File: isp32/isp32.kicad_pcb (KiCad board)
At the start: 2 copper layers, 55.5 x 48.5 mm, 99 parts, among them J1 BAT1, J10 LoRa_ANT, J12 Micro_SD_Card, J2 Switching, J3 USB_C_Receptacle_USB2.0, J4 ESP_JTAG, J5 GPS_ANT, J6 F0, J7 F1, J9 ANT, M1 Motor_Servo, M2 Motor_Servo, M3 Motor_Servo, M4 Motor_Servo, Q1 BSS138, Q2 BSS138, Q3 IRLML6402, Q4 BSS138, Q5 IRLML6402, Q6 S8050, SW1 RST, SW2 IO0, U1 SC189ZSKTRT, U10 BMP280, U11 MPU-9250, U2 USBLC6-2SC6, U3 STM32F030F4Px, U4 MP1660GTF-Z, U6 24LC32, U7 NEO-XM, U8 ESP32-S3-WROOM-1U, U9 RFM98W-315S2

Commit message: Rough route
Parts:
- added REF**: OSHW-Logo2_7.3x6mm_SilkScreen, Symbol:OSHW-Logo2_7.3x6mm_SilkScreen, F.Cu at (110.5, 79.2)
- C1, C10, C6, G***, L1, U1: moved to F.Cu
- C2, C4, C5, C7, C8, L3, LS1, Q6, R10, R11, R3, R33, R8, R9, TP2, U4: moved to B.Cu
- U3: value STM32F030F4Px -> STM32G030F6
- moved C10 48.5 mm to (123.2, 76.3)
- moved R10 45.8 mm to (118.8, 84.4), turned to -90 degrees
- moved G*** 45.7 mm to (129.8, 75.1), turned to 0 degrees
- moved R9 43.8 mm to (117.2, 84.4), turned to -90 degrees
- moved C6 42.5 mm to (120.2, 77.1)
- moved R11 42.4 mm to (118.5, 82.0), turned to 0 degrees
- moved R3 41.9 mm to (115.5, 84.4), turned to 90 degrees
- moved C7 40.6 mm to (118.5, 80.3), turned to 0 degrees
- moved C5 39.7 mm to (113.6, 84.4), turned to -90 degrees
- moved C3 39.3 mm to (121.3, 59.7), turned to -90 degrees
- moved R33 39.1 mm to (115.0, 62.7)
- moved Q6 38.2 mm to (114.9, 65.6), turned to -90 degrees
- moved U4 37.9 mm to (115.3, 81.2), turned to 0 degrees
- moved C13 37.0 mm to (138.7, 59.3)
- moved U6 36.9 mm to (133.7, 58.0)
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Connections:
- U3 pad 1: GND -> SCL
- U3 pad 11: unconnected-(U3-Pad11) -> SERVO0
- U3 pad 12: unconnected-(U3-Pad12) -> SERVO1
- U3 pad 13: unconnected-(U3-Pad13) -> SERVO2
- U3 pad 14: unconnected-(U3-Pad14) -> SERVO3
- U3 pad 15: GND -> unconnected-(U3-Pad15)
- U3 pad 16: +3V3 -> unconnected-(U3-Pad16)
- U3 pad 17: SCL -> unconnected-(U3-Pad17)
- U3 pad 18: SDA -> SWDIO
- U3 pad 19: SWDIO -> SWCLK
- U3 pad 2: unconnected-(U3-Pad2) -> SDA
- U3 pad 20: SWCLK -> unconnected-(U3-Pad20)
- U3 pad 4: RST -> +3V3
- U3 pad 5: +3V3 -> GND
- U3 pad 6: SERVO0 -> RST
- U3 pad 7: SERVO1 -> Buzz
- U3 pad 8: SERVO2 -> RGB
- U3 pad 9: SERVO3 -> unconnected-(U3-Pad9)
- U8 pad 39: Buzz -> unconnected-(U8-Pad39)
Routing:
- net +3V3: track 9.51 -> 239.7 mm, vias 0 -> 9
- net +5V: track 25.5 -> 163.7 mm, vias 1 -> 2
- net +BATT: track 10.8 -> 42.2 mm, vias 0 -> 1
- net IMU_INT: track 0.00 -> 14.4 mm
- net Net-(J10-Pad1): track 0.00 -> 11.4 mm, vias 0 -> 1
- net MISO: track 0.00 -> 11.0 mm
- net Net-(J6-Pad1): track 0.00 -> 8.88 mm
- net Net-(J7-Pad1): track 0.00 -> 8.70 mm
- net SCL: track 0.00 -> 8.30 mm
- net SDA: track 0.00 -> 6.84 mm
- net Net-(Q1-Pad3): track 0.00 -> 5.52 mm
- net Net-(Q4-Pad3): track 0.00 -> 5.52 mm
- net Net-(D3-Pad2): track 0.00 -> 5.38 mm
- net UD+: track 0.00 -> 5.15 mm
- net cc1: track 0.00 -> 5.09 mm, vias 0 -> 2
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- added copper zone on F.Cu, net +3V3
- added copper zone on B.Cu, net +5V
- added copper zone on F.Cu, net +5V
- added copper zone on B.Cu, net +BATT
- added copper zone on B.Cu, net Net-(C4-Pad2)
- added copper zone on F.Cu, net Net-(L1-Pad1)
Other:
- board size 55.5 x 48.5 mm -> 53 x 48 mm
- board text added: "Board's Info 48mm x 53mm M3 Screwhole Input 5V~16V BSD-3-Clause By @wilicw"

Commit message: Complete routing
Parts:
- R19: moved to B.Cu
- moved R19 2.18 mm to (108.6, 84.9)
- moved REF** 0.78 mm to (110.7, 80.0)
- moved G*** 0.08 mm to (129.8, 75.0)
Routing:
- net MOSI: track 1.34 -> 67.2 mm, vias 0 -> 4
- net SDA: track 6.84 -> 63.0 mm, vias 0 -> 5
- net SCL: track 8.30 -> 59.3 mm, vias 0 -> 4
- net MISO: track 11.0 -> 61.0 mm, vias 0 -> 4
- net SCK: track 1.33 -> 50.2 mm, vias 0 -> 2
- net EXT_INT: track 0.00 -> 45.7 mm, vias 0 -> 2
- net GND: track 0.53 -> 37.6 mm, vias 3 -> 474
- net LORA_SS: track 0.00 -> 32.2 mm, vias 0 -> 1
- net IO0: track 2.06 -> 32.3 mm, vias 1 -> 2
- net RGB: track 1.97 -> 30.6 mm, vias 0 -> 2
- net LORA_INT: track 0.00 -> 26.4 mm, vias 0 -> 1
- net FIRE0: track 1.99 -> 24.9 mm, vias 0 -> 2
- net RST: track 0.00 -> 21.7 mm, vias 0 -> 1
- net TX1: track 0.00 -> 21.0 mm, vias 0 -> 2
- net SERVO3: track 0.00 -> 20.9 mm
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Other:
- board text added: "Board's Info 48mm x 53mm M3 Screw Holes Input 5V~16V BSD-3-Clause By @wilicw"
- board text removed: "Board's Info 48mm x 53mm M3 Screwhole Input 5V~16V BSD-3-Clause By @wilicw"

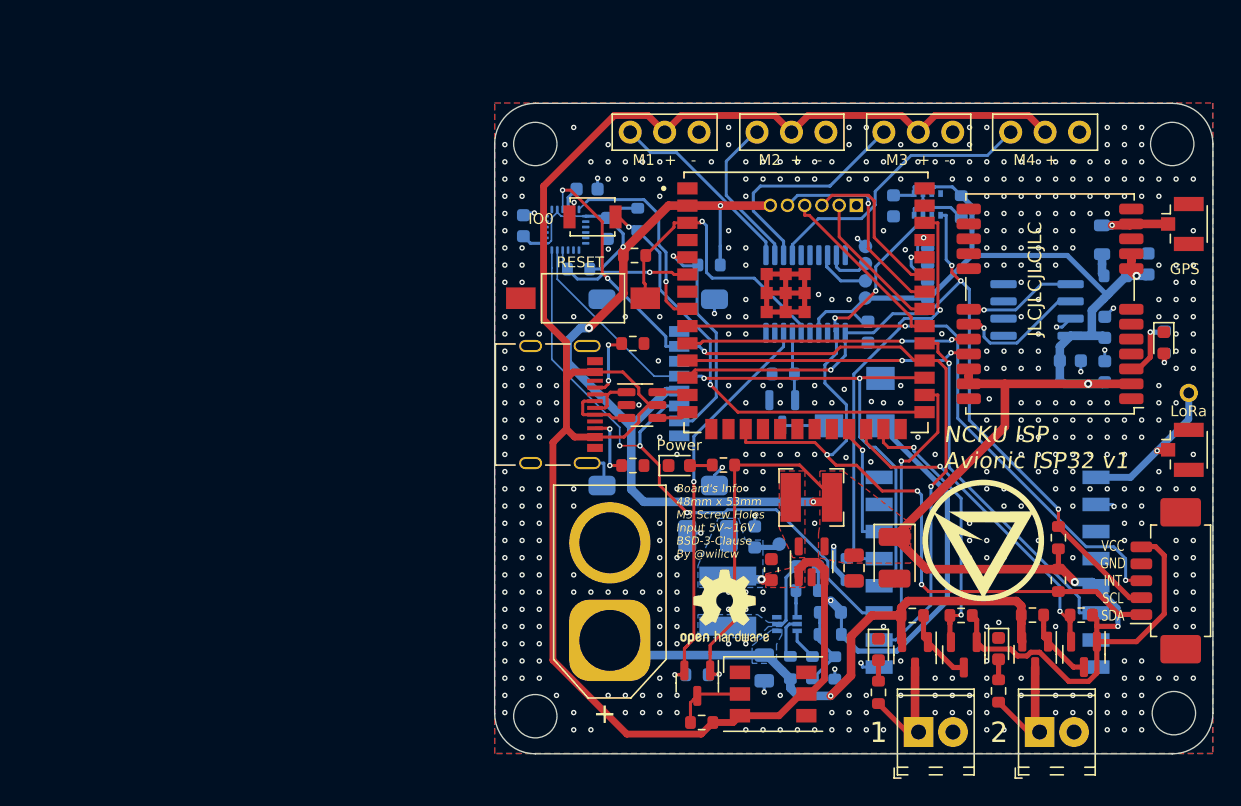
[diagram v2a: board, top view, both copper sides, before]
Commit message: Change label style
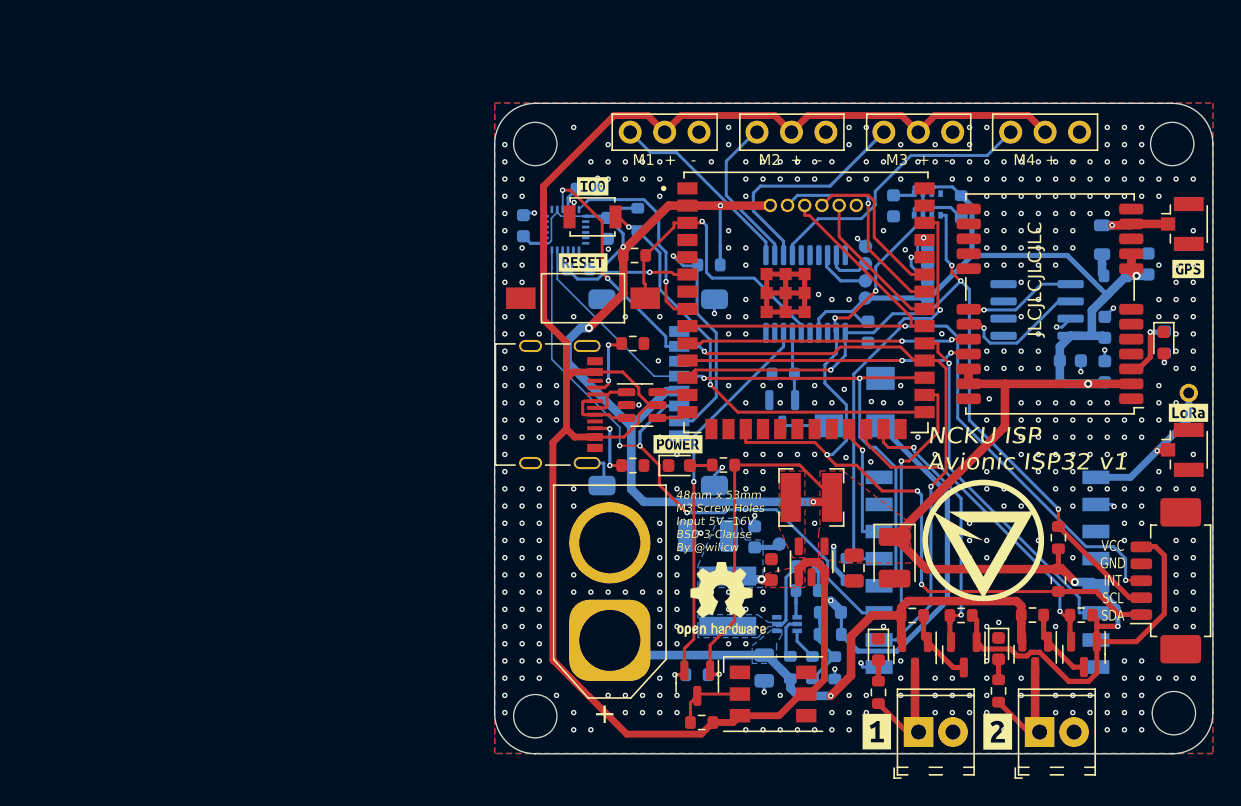
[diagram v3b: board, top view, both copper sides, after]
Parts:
- added kibuzzard-63CD04EB: G***, kibuzzard-63CD04EB, F.Cu at (121.9, 89.1)
- added kibuzzard-63CD04FB: G***, kibuzzard-63CD04FB, F.Cu at (130.8, 89.1)
- added kibuzzard-63CD1CED: G***, kibuzzard-63CD1CED, F.Cu at (100.2, 54.5)
- added kibuzzard-63CD1CF7: G***, kibuzzard-63CD1CF7, F.Cu at (100.9, 48.9)
- added kibuzzard-63CD1D24: G***, kibuzzard-63CD1D24, F.Cu at (107.2, 67.9)
- added kibuzzard-63CD1D2E: G***, kibuzzard-63CD1D2E, F.Cu at (144.9, 65.6)
- added kibuzzard-63CD1D37: G***, kibuzzard-63CD1D37, F.Cu at (144.9, 55.0)
- added kibuzzard-63CD1E61: G***, kibuzzard-63CD1E61, B.Cu at (123.0, 57.1)
- added kibuzzard-63CD1E61: G***, kibuzzard-63CD1E61, B.Cu at (127.6, 57.2)
- added kibuzzard-63CD1E6C: G***, kibuzzard-63CD1E6C, B.Cu at (127.6, 55.9)
- added kibuzzard-63CD1E76: G***, kibuzzard-63CD1E76, B.Cu at (127.6, 54.6)
- added kibuzzard-63CD1E7F: G***, kibuzzard-63CD1E7F, B.Cu at (127.6, 53.4)
- added kibuzzard-63CD1E7F: G***, kibuzzard-63CD1E7F, B.Cu at (123.0, 53.3)
- added kibuzzard-63CD1EC0: G***, kibuzzard-63CD1EC0, B.Cu at (123.0, 54.6)
- added kibuzzard-63CD1EC5: G***, kibuzzard-63CD1EC5, B.Cu at (123.0, 55.9)
- added kibuzzard-63CD1F56: G***, kibuzzard-63CD1F56, B.Cu at (120.4, 48.4)
- added kibuzzard-63CD1F64: G***, kibuzzard-63CD1F64, B.Cu at (119.1, 48.4)
- added kibuzzard-63CD1F6A: G***, kibuzzard-63CD1F6A, B.Cu at (117.9, 48.4)
- added kibuzzard-63CD1F72: G***, kibuzzard-63CD1F72, B.Cu at (116.6, 48.4)
- added kibuzzard-63CD1F77: G***, kibuzzard-63CD1F77, B.Cu at (115.3, 48.4)
- added kibuzzard-63CD1F7D: G***, kibuzzard-63CD1F7D, B.Cu at (114.0, 48.4)
- moved REF** 0.61 mm to (110.4, 79.4)
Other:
- board text added: "48mm x 53mm M3 Screw Holes Input 5V~16V BSD-3-Clause By @wilicw"
- board text added: "Designed in ROC (Taiwan)"
- board text removed: "1"
- board text removed: "2"
- board text removed: "Board's Info 48mm x 53mm M3 Screw Holes Input 5V~16V BSD-3-Clause By @wilicw"
- board text removed: "GND RXD TXD 3V3"
- board text removed: "GND SWCLK SWDIO 3V3"
- board text removed: "GND TDO TMS TCK TDI 3V3"
- board text removed: "GPS"
- board text removed: "IO0"
- board text removed: "LoRa"
- board text removed: "Power"
- board text removed: "RESET"

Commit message: Change label and panel size
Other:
- board text removed: "Designed in ROC (Taiwan)"
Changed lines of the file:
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@@
     (attr board_only exclude_from_pos_files exclude_from_bom)
     (fp_text reference "kibuzzard-63CD1D37" (at 0 -3.722793) (layer "F.SilkS") hide
-      (effects (font (size 0 0)))
+      (effects (font (size 0 0) (thickness 0.15)))
     )
     (fp_text value "G***" (at 0 3.722793) (layer "F.SilkS") hide
-      (effects (font (size 0 0)))
+      (effects (font (size 0 0) (thickness 0.15)))
     )
     (fp_poly (pts
@@
     (attr board_only exclude_from_pos_files exclude_from_bom)
     (fp_text reference "kibuzzard-63CD1CED" (at 0 -3.722793) (layer "F.SilkS") hide
-      (effects (font (size 0 0)))
+      (effects (font (size 0 0) (thickness 0.15)))
     )
     (fp_text value "G***" (at 0 3.722793) (layer "F.SilkS") hide
-      (effects (font (size 0 0)))
+      (effects (font (size 0 0) (thickness 0.15)))
     )
     (fp_poly (pts
@@
     (attr board_only exclude_from_pos_files exclude_from_bom)
     (fp_text reference "kibuzzard-63CD1CF7" (at 0 -3.722793) (layer "F.SilkS") hide
-      (effects (font (size 0 0)))
+      (effects (font (size 0 0) (thickness 0.15)))
     )
     (fp_text value "G***" (at 0 3.722793) (layer "F.SilkS") hide
-      (effects (font (size 0 0)))
+      (effects (font (size 0 0) (thickness 0.15)))
     )
     (fp_poly (pts
@@
     (attr board_only exclude_from_pos_files exclude_from_bom)
     (fp_text reference "kibuzzard-63CD1D2E" (at 0 -3.718348) (layer "F.SilkS") hide
-      (effects (font (size 0 0)))
+      (effects (font (size 0 0) (thickness 0.15)))
     )
     (fp_text value "G***" (at 0 3.718348) (layer "F.SilkS") hide
-      (effects (font (size 0 0)))
+      (effects (font (size 0 0) (thickness 0.15)))
     )
     (fp_poly (pts
@@
     (attr board_only exclude_from_pos_files exclude_from_bom)
     (fp_text reference "kibuzzard-63CD1D24" (at 0 -3.722793) (layer "F.SilkS") hide
-      (effects (font (size 0 0)))
+      (effects (font (size 0 0) (thickness 0.15)))
     )
     (fp_text value "G***" (at 0 3.722793) (layer "F.SilkS") hide
-      (effects (font (size 0 0)))
+      (effects (font (size 0 0) (thickness 0.15)))
     )
     (fp_poly (pts
@@
     (attr board_only exclude_from_pos_files exclude_from_bom)
     (fp_text reference "kibuzzard-63CD1E6C" (at 0 3.631777) (layer "B.SilkS") hide
-      (effects (font (size 0 0)) (justify mirror))
+      (effects (font (size 0 0) (thickness 0.15)) (justify mirror))
     )
     (fp_text value "G***" (at 0 -3.631777) (layer "B.SilkS") hide
-      (effects (font (size 0 0)) (justify mirror))
+      (effects (font (size 0 0) (thickness 0.15)) (justify mirror))
     )
     (fp_poly (pts
@@
     (attr board_only exclude_from_pos_files exclude_from_bom)
     (fp_text reference "kibuzzard-63CD1EC0" (at 0 3.638444) (layer "B.SilkS") hide
-      (effects (font (size 0 0)) (justify mirror))
+      (effects (font (size 0 0) (thickness 0.15)) (justify mirror))
     )
     (fp_text value "G***" (at 0 -3.638444) (layer "B.SilkS") hide
-      (effects (font (size 0 0)) (justify mirror))
+      (effects (font (size 0 0) (thickness 0.15)) (justify mirror))
     )
     (fp_poly (pts
@@
     (attr board_only exclude_from_pos_files exclude_from_bom)
     (fp_text reference "kibuzzard-63CD1F64" (at 0 3.638444 90) (layer "B.SilkS") hide
-      (effects (font (size 0 0)) (justify mirror))
+      (effects (font (size 0 0) (thickness 0.15)) (justify mirror))
     )
     (fp_text value "G***" (at 0 -3.638444 90) (layer "B.SilkS") hide
-      (effects (font (size 0 0)) (justify mirror))
+      (effects (font (size 0 0) (thickness 0.15)) (justify mirror))
     )
     (fp_poly (pts
@@
     (attr board_only exclude_from_pos_files exclude_from_bom)
     (fp_text reference "kibuzzard-63CD1E76" (at 0 3.631777) (layer "B.SilkS") hide
-      (effects (font (size 0 0)) (justify mirror))
+      (effects (font (size 0 0) (thickness 0.15)) (justify mirror))
     )
     (fp_text value "G***" (at 0 -3.631777) (layer "B.SilkS") hide
-      (effects (font (size 0 0)) (justify mirror))
+      (effects (font (size 0 0) (thickness 0.15)) (justify mirror))
     )
     (fp_poly (pts
@@
     (attr board_only exclude_from_pos_files exclude_from_bom)
     (fp_text reference "kibuzzard-63CD1E7F" (at 0 3.638444) (layer "B.SilkS") hide
-      (effects (font (size 0 0)) (justify mirror))
+      (effects (font (size 0 0) (thickness 0.15)) (justify mirror))
     )
     (fp_text value "G***" (at 0 -3.638444) (layer "B.SilkS") hide
-      (effects (font (size 0 0)) (justify mirror))
+      (effects (font (size 0 0) (thickness 0.15)) (justify mirror))
     )
     (fp_poly (pts
@@
     (attr board_only exclude_from_pos_files exclude_from_bom)
     (fp_text reference "kibuzzard-63CD1E61" (at 0 3.638444) (layer "B.SilkS") hide
-      (effects (font (size 0 0)) (justify mirror))
+      (effects (font (size 0 0) (thickness 0.15)) (justify mirror))
     )
     (fp_text value "G***" (at 0 -3.638444) (layer "B.SilkS") hide
-      (effects (font (size 0 0)) (justify mirror))
+      (effects (font (size 0 0) (thickness 0.15)) (justify mirror))
     )
     (fp_poly (pts
@@
     (attr board_only exclude_from_pos_files exclude_from_bom)
     (fp_text reference "kibuzzard-63CD1F6A" (at 0 3.638444 90) (layer "B.SilkS") hide
-      (effects (font (size 0 0)) (justify mirror))
+      (effects (font (size 0 0) (thickness 0.15)) (justify mirror))
     )
     (fp_text value "G***" (at 0 -3.638444 90) (layer "B.SilkS") hide
-      (effects (font (size 0 0)) (justify mirror))
+      (effects (font (size 0 0) (thickness 0.15)) (justify mirror))
     )
     (fp_poly (pts
@@
     (attr board_only exclude_from_pos_files exclude_from_bom)
     (fp_text reference "kibuzzard-63CD1E7F" (at 0 3.638444) (layer "B.SilkS") hide
-      (effects (font (size 0 0)) (justify mirror))
+      (effects (font (size 0 0) (thickness 0.15)) (justify mirror))
     )
     (fp_text value "G***" (at 0 -3.638444) (layer "B.SilkS") hide
-      (effects (font (size 0 0)) (justify mirror))
+      (effects (font (size 0 0) (thickness 0.15)) (justify mirror))
     )
     (fp_poly (pts
@@
     (attr board_only exclude_from_pos_files exclude_from_bom)
     (fp_text reference "kibuzzard-63CD1EC5" (at 0 3.638444) (layer "B.SilkS") hide
-      (effects (font (size 0 0)) (justify mirror))
+      (effects (font (size 0 0) (thickness 0.15)) (justify mirror))
     )
     (fp_text value "G***" (at 0 -3.638444) (layer "B.SilkS") hide
-      (effects (font (size 0 0)) (justify mirror))
+      (effects (font (size 0 0) (thickness 0.15)) (justify mirror))
     )
     (fp_poly (pts
@@
     (attr board_only exclude_from_pos_files exclude_from_bom)
     (fp_text reference "kibuzzard-63CD1F56" (at 0 3.638444 90) (layer "B.SilkS") hide
-      (effects (font (size 0 0)) (justify mirror))
+      (effects (font (size 0 0) (thickness 0.15)) (justify mirror))
     )
     (fp_text value "G***" (at 0 -3.638444 90) (layer "B.SilkS") hide
-      (effects (font (size 0 0)) (justify mirror))
+      (effects (font (size 0 0) (thickness 0.15)) (justify mirror))
     )
     (fp_poly (pts
@@
     (attr board_only exclude_from_pos_files exclude_from_bom)
     (fp_text reference "kibuzzard-63CD1F77" (at 0 3.631777 90) (layer "B.SilkS") hide
-      (effects (font (size 0 0)) (justify mirror))
+      (effects (font (size 0 0) (thickness 0.15)) (justify mirror))
     )
     (fp_text value "G***" (at 0 -3.631777 90) (layer "B.SilkS") hide
-      (effects (font (size 0 0)) (justify mirror))
+      (effects (font (size 0 0) (thickness 0.15)) (justify mirror))
     )
     (fp_poly (pts
@@
     (attr board_only exclude_from_pos_files exclude_from_bom)
     (fp_text reference "kibuzzard-63CD1F7D" (at 0 3.638444 90) (layer "B.SilkS") hide
-      (effects (font (size 0 0)) (justify mirror))
+      (effects (font (size 0 0) (thickness 0.15)) (justify mirror))
     )
     (fp_text value "G***" (at 0 -3.638444 90) (layer "B.SilkS") hide
-      (effects (font (size 0 0)) (justify mirror))
+      (effects (font (size 0 0) (thickness 0.15)) (justify mirror))
     )
     (fp_poly (pts
@@
     (attr board_only exclude_from_pos_files exclude_from_bom)
     (fp_text reference "kibuzzard-63CD1F72" (at 0 3.638444 90) (layer "B.SilkS") hide
-      (effects (font (size 0 0)) (justify mirror))
+      (effects (font (size 0 0) (thickness 0.15)) (justify mirror))
     )
     (fp_text value "G***" (at 0 -3.638444 90) (layer "B.SilkS") hide
-      (effects (font (size 0 0)) (justify mirror))
+      (effects (font (size 0 0) (thickness 0.15)) (justify mirror))
     )
     (fp_poly (pts
@@
     (attr board_only exclude_from_pos_files exclude_from_bom)
     (fp_text reference "kibuzzard-63CD1E61" (at 0 3.638444) (layer "B.SilkS") hide
-      (effects (font (size 0 0)) (justify mirror))
+      (effects (font (size 0 0) (thickness 0.15)) (justify mirror))
     )
     (fp_text value "G***" (at 0 -3.638444) (layer "B.SilkS") hide
-      (effects (font (size 0 0)) (justify mirror))
+      (effects (font (size 0 0) (thickness 0.15)) (justify mirror))
     )
     (fp_poly (pts
@@
   (gr_arc (start 146.700008 87.77498) (mid 145.82133 89.896307) (end 143.700008 90.77498) (layer "Edge.Cuts") (width 0.1))
   (gr_line (start 93.7 74.77498) (end 93.7 55.27498) (layer "Edge.Cuts") (width 0.1))
-  (gr_text "Designed in ROC (Taiwan)" (at 111.63 88.07) (layer "B.SilkS")
-    (effects (font (size 0.8 0.8) (thickness 0.15) italic) (justify mirror))
-  )
   (gr_text "5v" (at 116.6 75.4) (layer "B.SilkS")
     (effects (font (size 0.6 0.6) (thickness 0.1)) (justify mirror))
@@
   )
   (gr_text "VCC\nGND\nINT\nSCL\nSDA" (at 139.32132 78.00366) (layer "F.SilkS")
-    (effects (font (size 0.8 0.6) (thickness 0.15)))
+    (effects (font (size 0.8 0.6) (thickness 0.127)))
   )
   (gr_text "JLCJLCJLCJLC" (at 133.57132 55.75366 90) (layer "F.SilkS")
